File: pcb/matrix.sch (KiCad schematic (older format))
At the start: 165 parts, among them SW0 SW_Push, SW1 SW_Push, SW10 SW_Push, SW11 SW_Push, SW12 SW_Push, SW13 SW_Push, SW14 SW_Push, SW15 SW_Push, SW16 SW_Push, SW17 SW_Push, SW18 SW_Push, SW19 SW_Push, SW2 SW_Push, SW20 SW_Push, SW21 SW_Push, SW22 SW_Push, SW23 SW_Push, SW24 SW_Push, SW25 SW_Push, SW26 SW_Push, SW27 SW_Push, SW28 SW_Push, SW29 SW_Push, SW3 SW_Push, SW30 SW_Push, SW31 SW_Push, SW32 SW_Push, SW33 SW_Push, SW34 SW_Push, SW35 SW_Push, SW36 SW_Push, SW37 SW_Push, SW38 SW_Push, SW39 SW_Push, SW3s1 SW_Push, SW4 SW_Push, SW40 SW_Push, SW41 SW_Push, SW42 SW_Push, SW43 SW_Push, SW44 SW_Push, SW45 SW_Push, SW46 SW_Push, SW47 SW_Push, SW48 SW_Push, SW49 SW_Push, SW5 SW_Push, SW50 SW_Push, SW51 SW_Push, SW52 SW_Push, SW53 SW_Push, SW54 SW_Push, SW55 SW_Push, SW56 SW_Push, SW57 SW_Push, SW58 SW_Push, SW59 SW_Push, SW6 SW_Push, SW60 SW_Push, SW61 SW_Push, SW62 SW_Push, SW63 SW_Push, SW64 SW_Push, SW65 SW_Push, SW66 SW_Push, SW67 SW_Push, SW68 SW_Push, SW69 SW_Push, SW7 SW_Push, SW70 SW_Push, SW71 SW_Push, SW72 SW_Push, SW73 SW_Push, SW74 SW_Push, SW75 SW_Push, SW76 SW_Push, SW77 SW_Push, SW78 SW_Push, SW79 SW_Push, SW8 SW_Push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

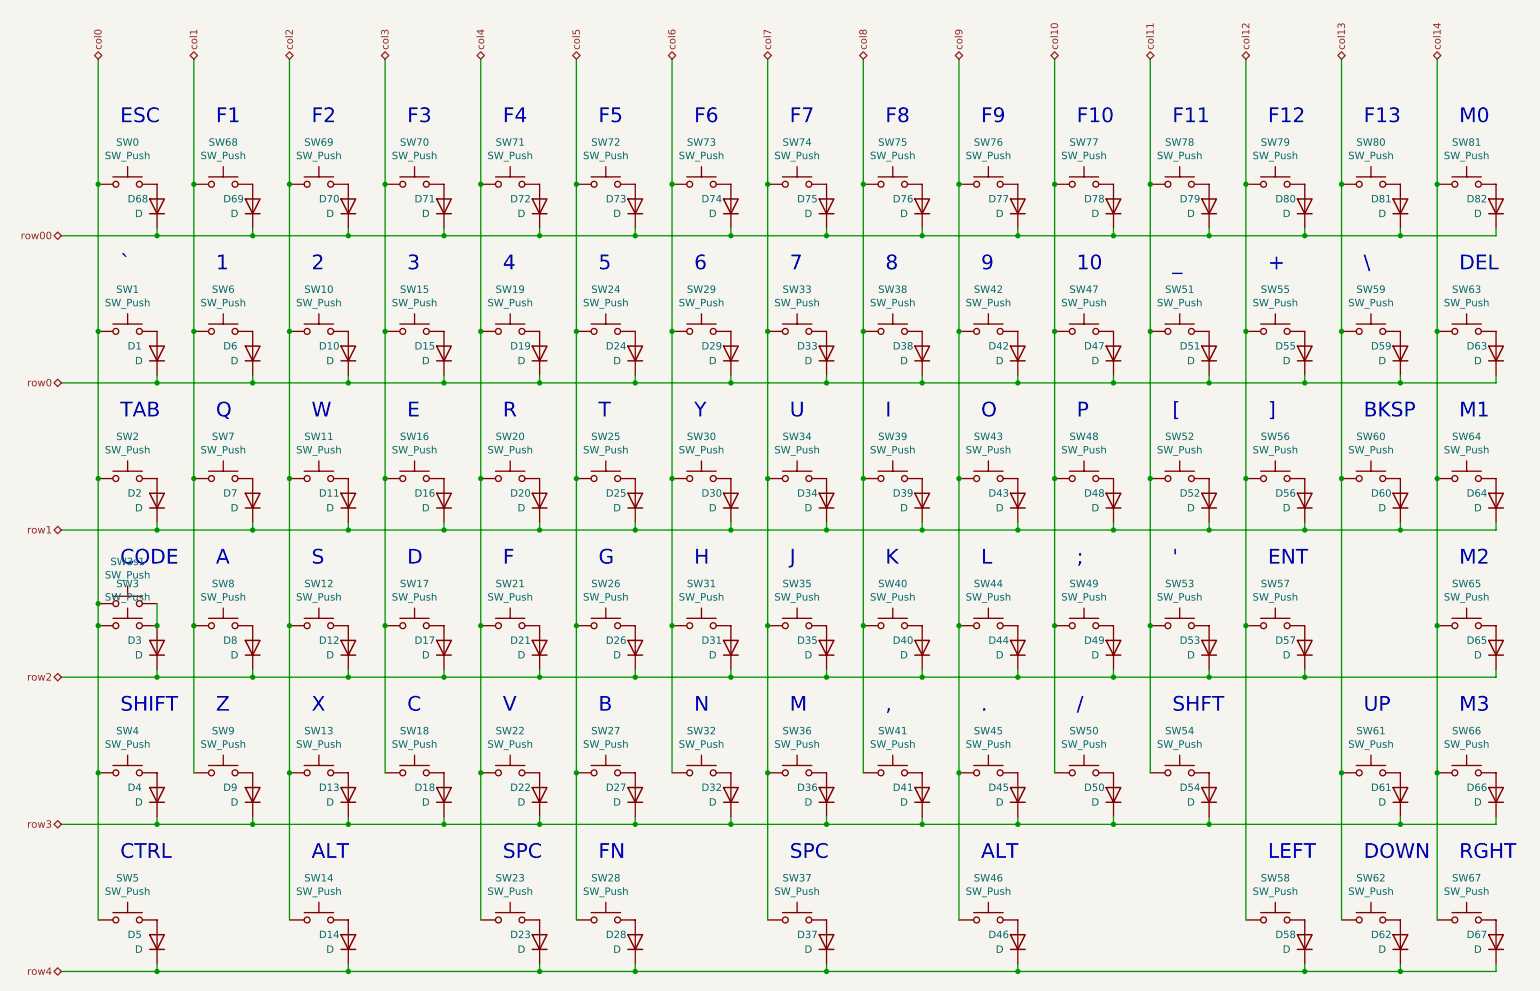
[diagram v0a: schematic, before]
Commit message: updated pcb labels to be more consistent [v1.0.1]
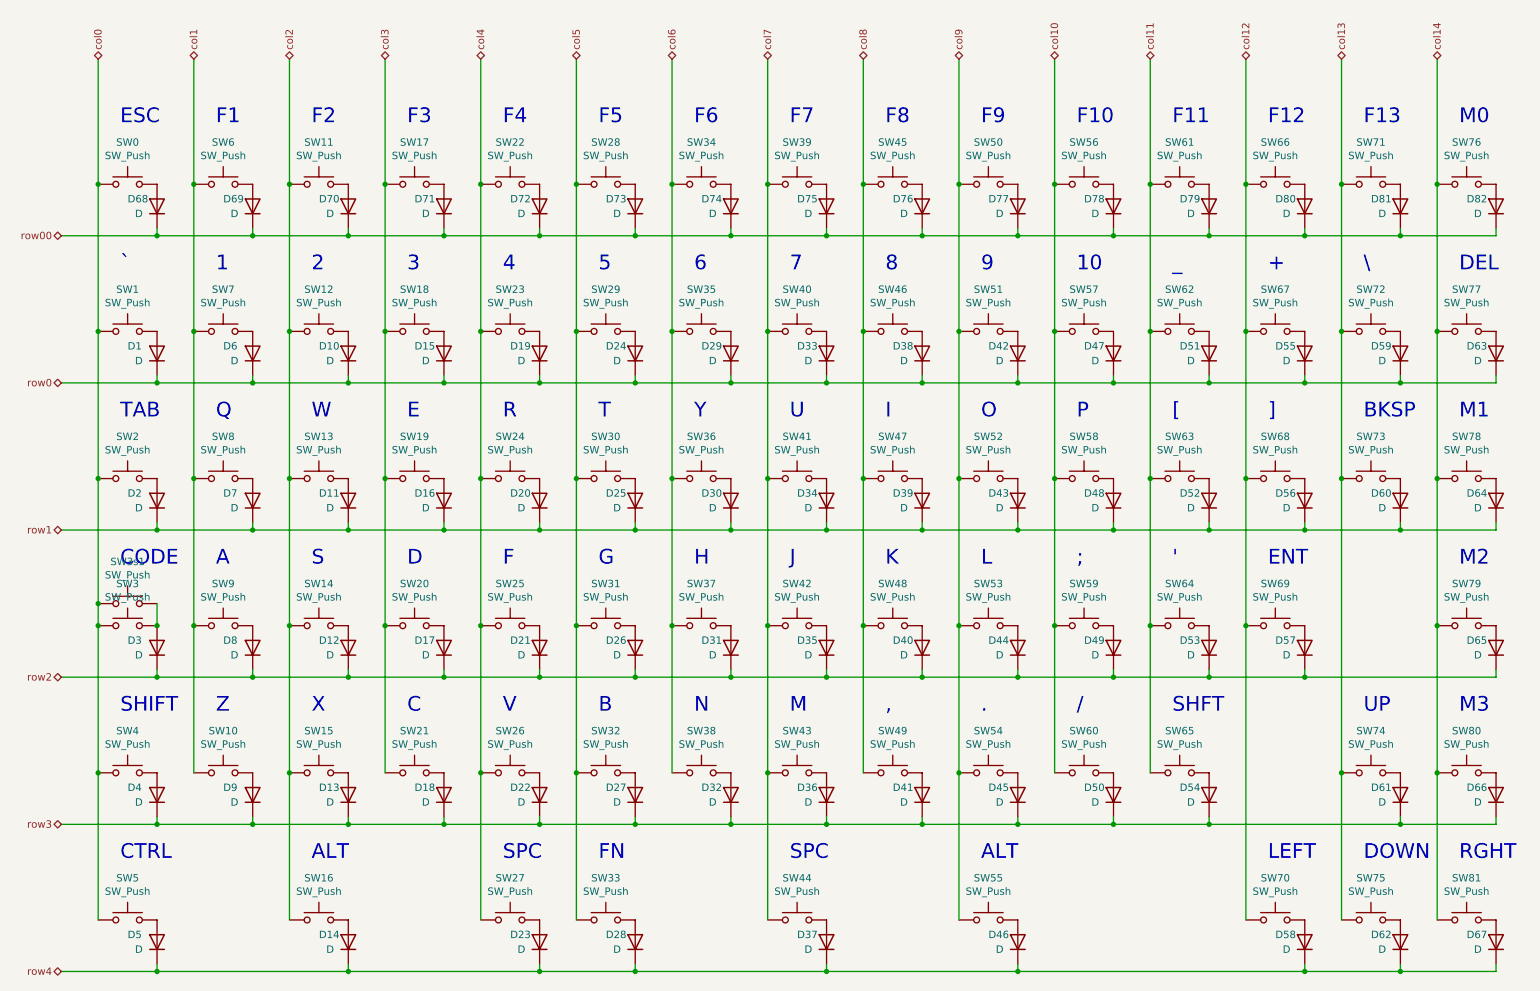
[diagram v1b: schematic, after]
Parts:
- renumbered SW9 to SW10, SW69 to SW11, SW10 to SW12, SW11 to SW13, SW12 to SW14, SW13 to SW15, SW14 to SW16, SW70 to SW17, SW15 to SW18, SW16 to SW19, SW17 to SW20, SW18 to SW21, SW71 to SW22, SW19 to SW23, SW20 to SW24, SW21 to SW25, SW22 to SW26, SW23 to SW27, SW72 to SW28, SW24 to SW29, SW25 to SW30, SW26 to SW31, SW27 to SW32, SW28 to SW33, SW73 to SW34, SW29 to SW35, SW30 to SW36, SW31 to SW37, SW32 to SW38, SW74 to SW39, SW33 to SW40, SW34 to SW41, SW35 to SW42, SW36 to SW43, SW37 to SW44, SW75 to SW45, SW38 to SW46, SW39 to SW47, SW40 to SW48, SW41 to SW49, SW76 to SW50, SW42 to SW51, SW43 to SW52, SW44 to SW53, SW45 to SW54, SW46 to SW55, SW77 to SW56, SW47 to SW57, SW48 to SW58, SW49 to SW59, SW68 to SW6, SW50 to SW60, SW78 to SW61, SW51 to SW62, SW52 to SW63, SW53 to SW64, SW54 to SW65, SW79 to SW66, SW55 to SW67, SW56 to SW68, SW57 to SW69, SW6 to SW7, SW58 to SW70, SW80 to SW71, SW59 to SW72, SW60 to SW73, SW61 to SW74, SW62 to SW75, SW81 to SW76, SW63 to SW77, SW64 to SW78, SW65 to SW79, SW7 to SW8, SW66 to SW80, SW67 to SW81, SW8 to SW9
